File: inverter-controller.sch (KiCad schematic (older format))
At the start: 0 parts

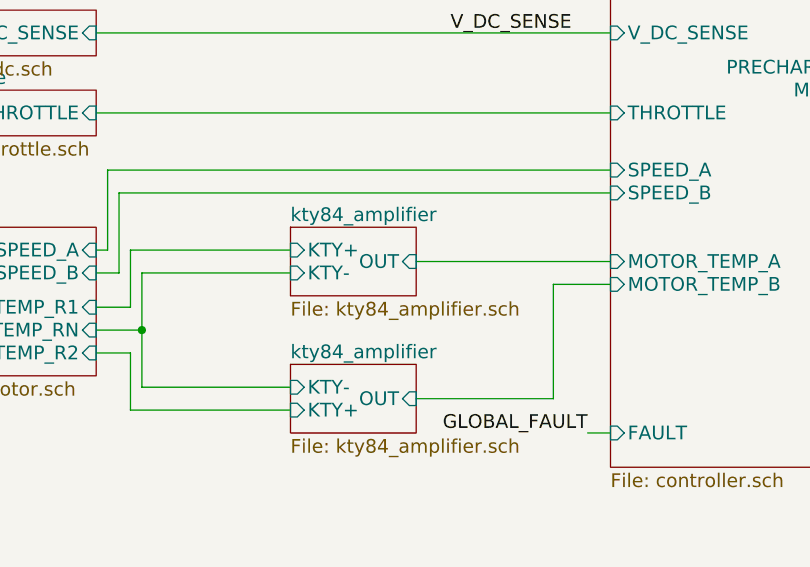
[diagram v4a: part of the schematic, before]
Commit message: Deduping kty_84 sheet names.
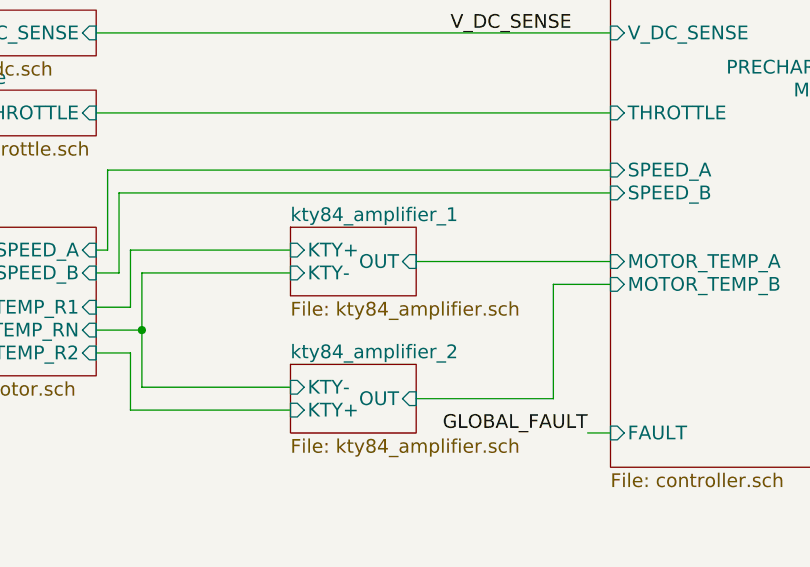
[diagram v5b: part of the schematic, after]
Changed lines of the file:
@@
 S 3450 2700 550  300
 U 5AF6F00C
-F0 "kty84_amplifier" 60
+F0 "kty84_amplifier_1" 60
 F1 "kty84_amplifier.sch" 60
 F2 "KTY+" I L 3450 2800 60
@@
 S 3450 3300 550  300
 U 5AF71A27
-F0 "kty84_amplifier" 60
+F0 "kty84_amplifier_2" 60
 F1 "kty84_amplifier.sch" 60
 F2 "KTY+" I L 3450 3500 60
